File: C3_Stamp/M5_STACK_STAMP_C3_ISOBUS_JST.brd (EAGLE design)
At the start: 20.3 x 35.6 mm, 3 parts, among them J1 61300811121, J2 61300611121

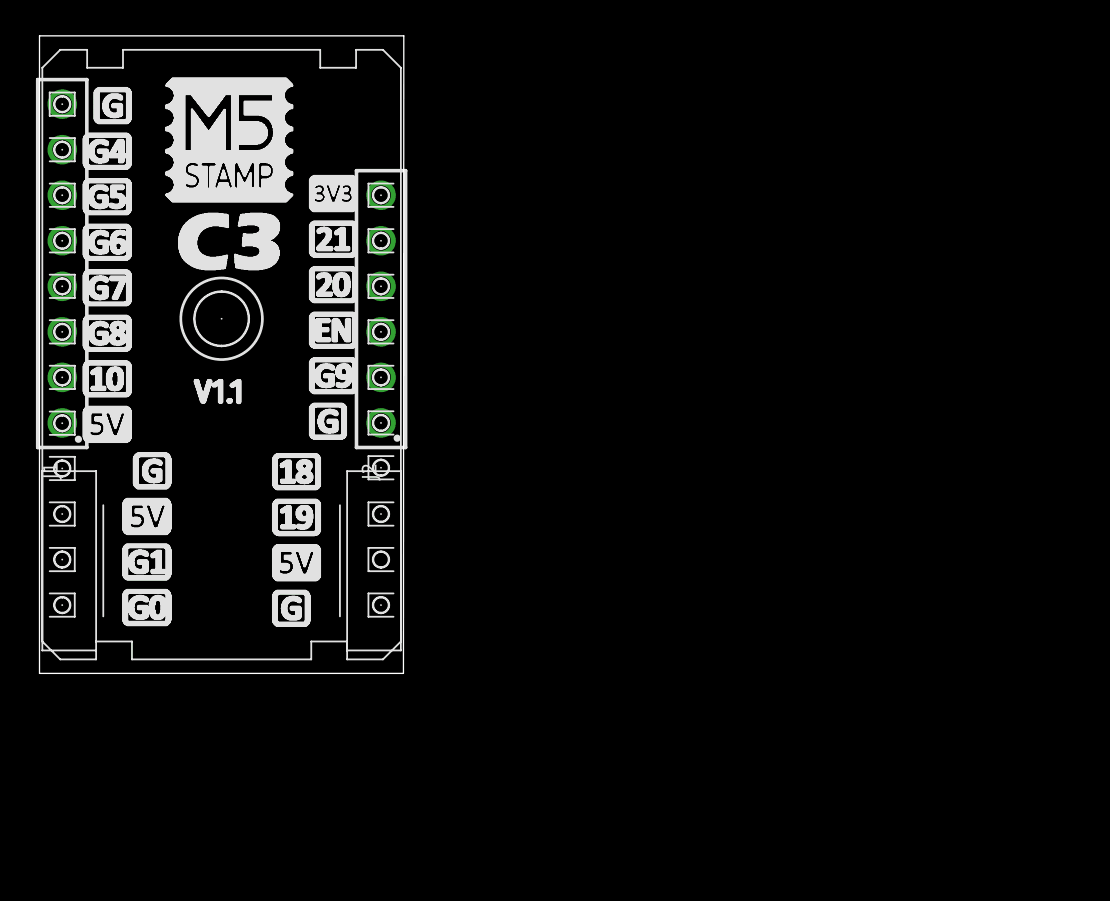
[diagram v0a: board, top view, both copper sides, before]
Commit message: 2 different Connectors.
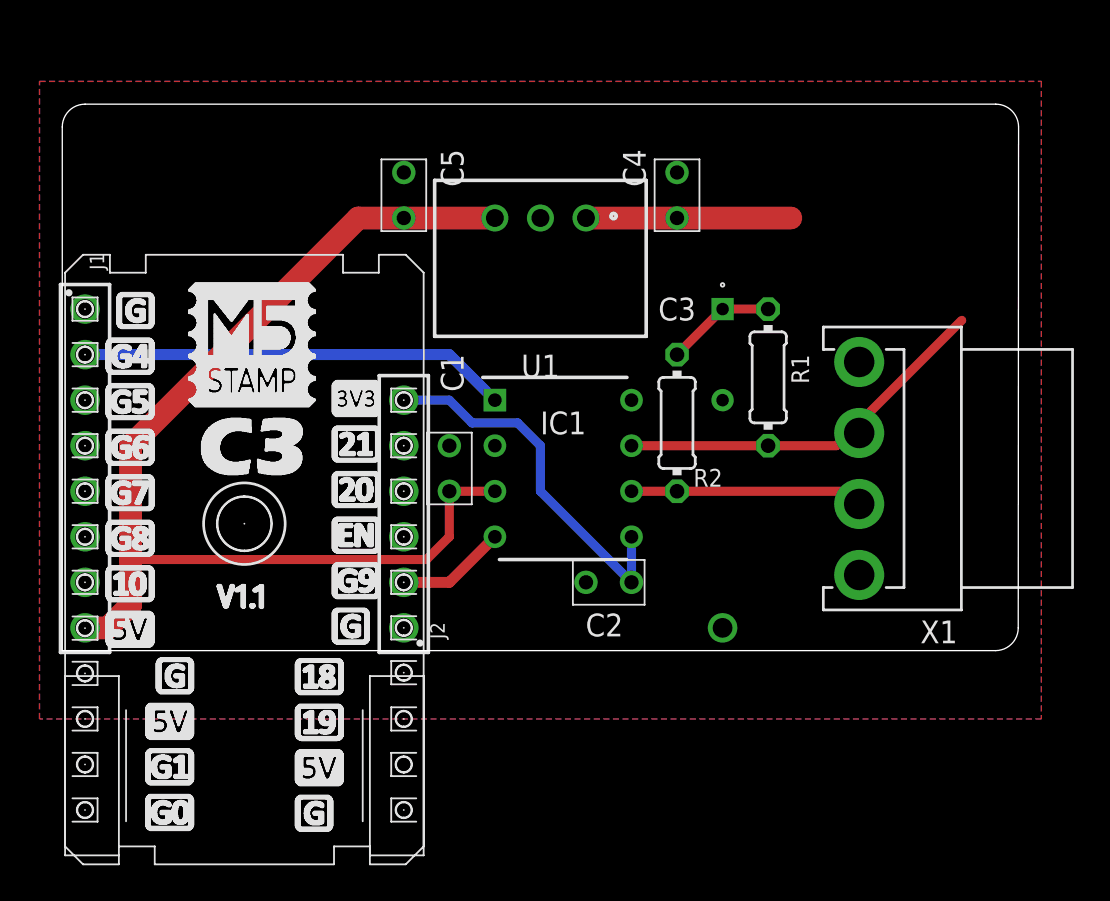
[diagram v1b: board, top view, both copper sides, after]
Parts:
- added C1, C2, C4, C5: FG18X7R1H104KNT06, FG18X7R1H104KNT06-pcb-part-libraries:FG18C0G1H101JNT06
- added C3: FG28X7R1H473KNT06, FG28X7R1H473KNT06-pcb-part-libraries:FG28
- added IC1: MCP2562-E_P, MCP2562-E_P-pcb-part-libraries:DIP781W56P254L950H533Q8N
- added R1, R2: (no value), resistor:0204/7
- added U1: (no value), Wurth_Step Down Converter_MagI³C-FDSM:MAGI³C-FDSM_173XXXX42
- added X1: S4P-VH, con-JST VH:S4P-VH
- moved J1 11.5 mm to (2.54, 11.4), turned to 270 degrees
- moved J2 11.5 mm to (20.3, 8.89)
- moved U$1 11.5 mm to (2.54, 20.3)
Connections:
- new net +12V: C4.2, U1.1, X1.2
- new net +3V3: C2.2, IC1.5, J2.6
- new net +5V: C1.2, C5.2, IC1.3, J1.8, U1.3
- new net CAN_N: IC1.6, R2.1, X1.4
- new net CAN_P: IC1.7, R1.2, X1.3
- new net EN: J2.3
- new net G10: J1.7
- new net G20: J2.4
- new net G21: J2.5
- new net G4: IC1.1, J1.2
- new net G5: J1.3
- new net G6: J1.4
- new net G7: J1.5
- new net G8: J1.6
- new net G9: IC1.4, J2.2
- new net GND: C1.1, C2.1, C3.2, C4.1, C5.1, IC1.2, IC1.8, J1.1, J2.1, U1.2, X1.1
- new net N$1: C3.1, R1.1, R2.2
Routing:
- net +5V: track 0.00 -> 60.9 mm
- net G4: track 0.00 -> 23.9 mm
- net CAN_P: track 0.00 -> 21.3 mm
- net +3V3: track 0.00 -> 20.9 mm
- net CAN_N: track 0.00 -> 12.9 mm
- net +12V: track 0.00 -> 11.4 mm
- net G9: track 0.00 -> 6.13 mm
- net N$1: track 0.00 -> 6.13 mm
- added copper zone on layer 1, net GND
- added copper zone on layer 16, net GND
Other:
- board size 20.3 x 35.6 mm -> 53.3 x 30.5 mm
